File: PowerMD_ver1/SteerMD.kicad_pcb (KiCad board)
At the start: 2 copper layers, 75 x 88 mm, 230 parts, among them P1 SWD, P10 OUT_1, P11 ENC_0, P13 ENC_1, P14 I/O_1, P15 OUT_0, P2 MOTOR_COOLING, P3 CAN, P4 CAN, P5 SERIAL, P6 I/O_0, P7 FAN, P8 BATT_IN, P9 BATT_IN, Q1 MOSFET_N, Q2 MOSFET_N, Q3 MOSFET_N, Q4 MOSFET_N, Q5 MOSFET_N, Q6 MOSFET_N, Q7 MOSFET_N, Q8 MOSFET_N, SW1 RST, SW3 SW0, SW4 SW1, U1 MAX3051, U10 ACS758, U11 POWER_ON, U12 SI8274, U13 ACS758, U14 SI8274, U15 AZ1086H, U16 LOGO, U17 AQM0802, U18 LTC2644, U19 ADRESS, U2 BD9G101, U3 STM32F405RG, U4 SI8274, U5 SI8900, U6 ADC_~RST, U7 BD9G101G, U8 SI8274, U9 BD33FA1, Y1 8MHz

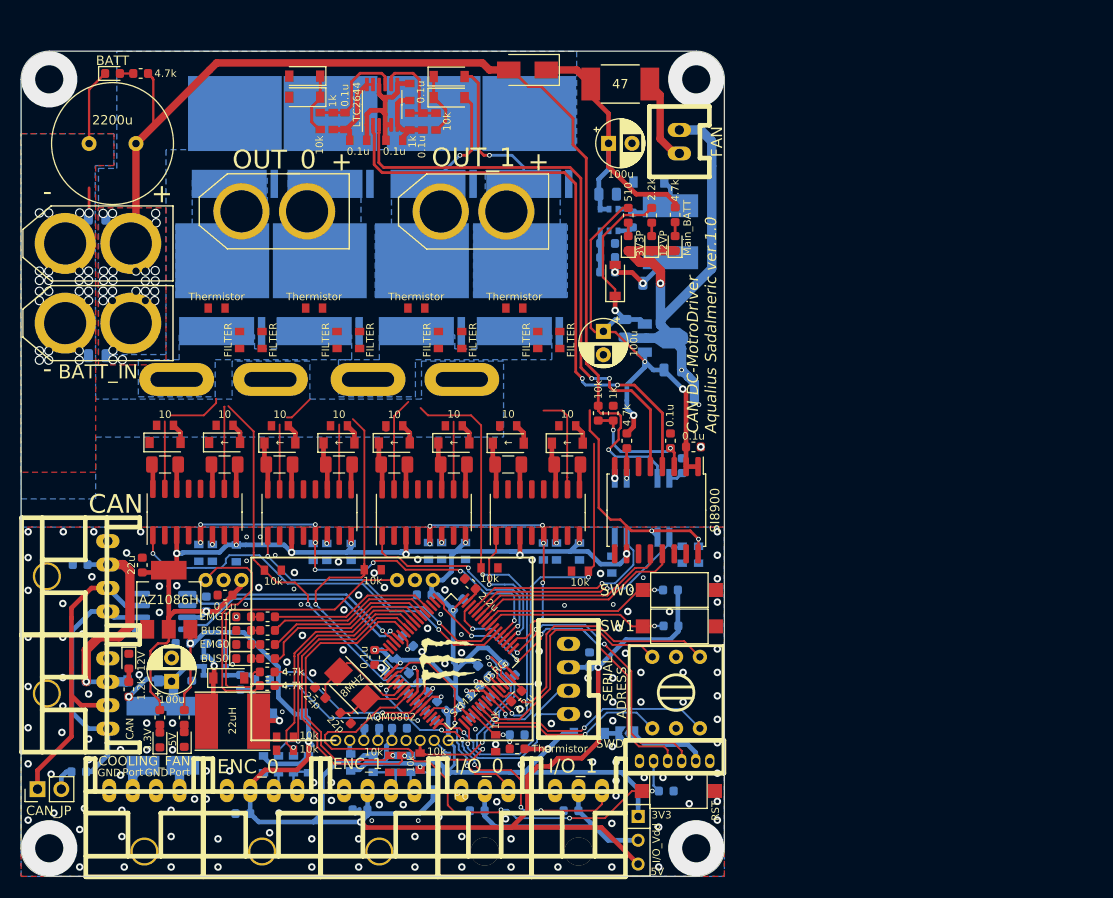
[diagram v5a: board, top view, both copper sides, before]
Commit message: ローサイドセンシングバージョンのMDも一応できた
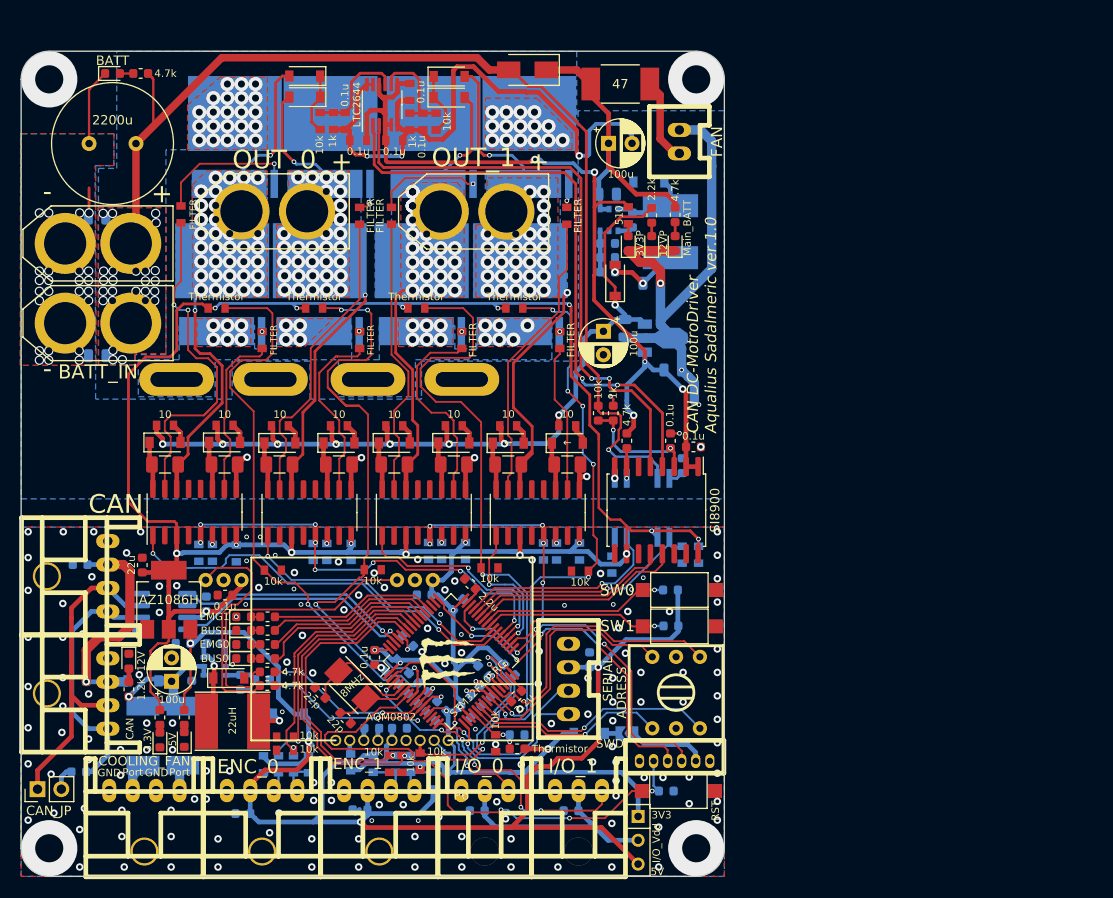
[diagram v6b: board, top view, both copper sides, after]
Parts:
- R34: footprint Resistor_SMD:R_0603_1608Metric -> Mizz_lib:1608_WP
- moved R17 14.8 mm to (89.5, 68.4)
- moved R53 14.2 mm to (112.0, 68.5)
- moved R63 13.6 mm to (130.7, 68.5)
- moved R30 13.5 mm to (108.6, 68.5)
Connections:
- C20 pad 2: /MOTOR0_BATT -> GNDPWR
- C31 pad 2: /MOTOR0_BATT -> GNDPWR
- C46 pad 2: /MOTOR1_BATT -> GNDPWR
- C49 pad 2: /MOTOR1_BATT -> GNDPWR
- U12 pad 9: /MOTOR0_BATT -> GNDPWR
- U14 pad 9: /MOTOR1_BATT -> GNDPWR
- U4 pad 9: /MOTOR0_BATT -> GNDPWR
- U8 pad 9: /MOTOR1_BATT -> GNDPWR
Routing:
- net +3V3: track 236.2 -> 329.2 mm, vias 20 -> 25
- net +12P: track 21.8 -> 94.5 mm, vias 1 -> 9
- net GNDPWR: track 86.2 -> 152.5 mm, vias 29 -> 38
- net /OUT0_L: track 4.20 -> 49.8 mm, vias 0 -> 36
- net /OUT0_R: track 2.64 -> 36.6 mm, vias 0 -> 33
- net Net-(R63-Pad2): track 0.00 -> 31.2 mm
- net +3.3VP: track 63.5 -> 93.2 mm, vias 3 -> 5
- net Net-(R17-Pad2): track 13.0 -> 38.6 mm, vias 0 -> 2
- net /Motor0R_Tmp: track 43.3 -> 67.9 mm, vias 2 -> 4
- net /OUT1_R: track 18.9 -> 43.1 mm, vias 1 -> 30
- net Net-(R30-Pad2): track 10.1 -> 32.9 mm
- net /OUT1_L: track 14.7 -> 36.1 mm, vias 1 -> 24
- net /Motor1R_Tmp: track 43.9 -> 64.5 mm, vias 3 -> 7
- net Net-(R53-Pad2): track 9.91 -> 30.0 mm
- net /Motor1L_Tmp: track 50.5 -> 69.3 mm
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- added copper zone on F.Cu, net /MOTOR0_BATT
- added copper zone on F.Cu, net /MOTOR1_BATT
- added copper zone on F.Cu, net /OUT0_L
- added copper zone on F.Cu, net /OUT0_R
- added copper zone on F.Cu, net /OUT1_L
- added copper zone on F.Cu, net /OUT1_R

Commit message: 電流制御MDをだいぶ進めた
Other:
- board text added: "Vdd"
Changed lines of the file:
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@@
     (effects (font (size 0.8 0.8) (thickness 0.15)))
   )
-  (gr_text 5V (at 121.95 127.2 90) (layer B.SilkS)
+  (gr_text Vdd (at 121.9 127.95) (layer B.SilkS)
     (effects (font (size 0.8 0.8) (thickness 0.15)) (justify mirror))
   )
@@
     (effects (font (size 0.8 0.8) (thickness 0.15)) (justify mirror))
   )
-  (gr_text GND (at 119.5 127.2 90) (layer B.SilkS)
+  (gr_text GND (at 119.5 127.95) (layer B.SilkS)
     (effects (font (size 0.8 0.8) (thickness 0.15)) (justify mirror))
   )
-  (gr_text I/O (at 124.5 127.2 90) (layer B.SilkS)
+  (gr_text I/O (at 124.5 127.95) (layer B.SilkS)
     (effects (font (size 0.8 0.8) (thickness 0.15)) (justify mirror))
   )
@@
     (effects (font (size 0.8 0.8) (thickness 0.15)) (justify mirror))
   )
-  (gr_text 5V (at 132 128) (layer B.SilkS)
+  (gr_text Vdd (at 132 128) (layer B.SilkS)
     (effects (font (size 0.8 0.8) (thickness 0.15)) (justify mirror))
   )
